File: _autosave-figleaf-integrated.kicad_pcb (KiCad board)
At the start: 2 copper layers, 145 x 105 mm, 62 parts, among them J2 HRO_TYPE-C-31-M-14, J3 Battery, J9 TC2030_SWD, Q2 2N7002, SW1 PWR, SW2 RST, U1 SRV05-4, U10 MAX17048, U3 BQ24075, U8 nRF52840_moko_mk08

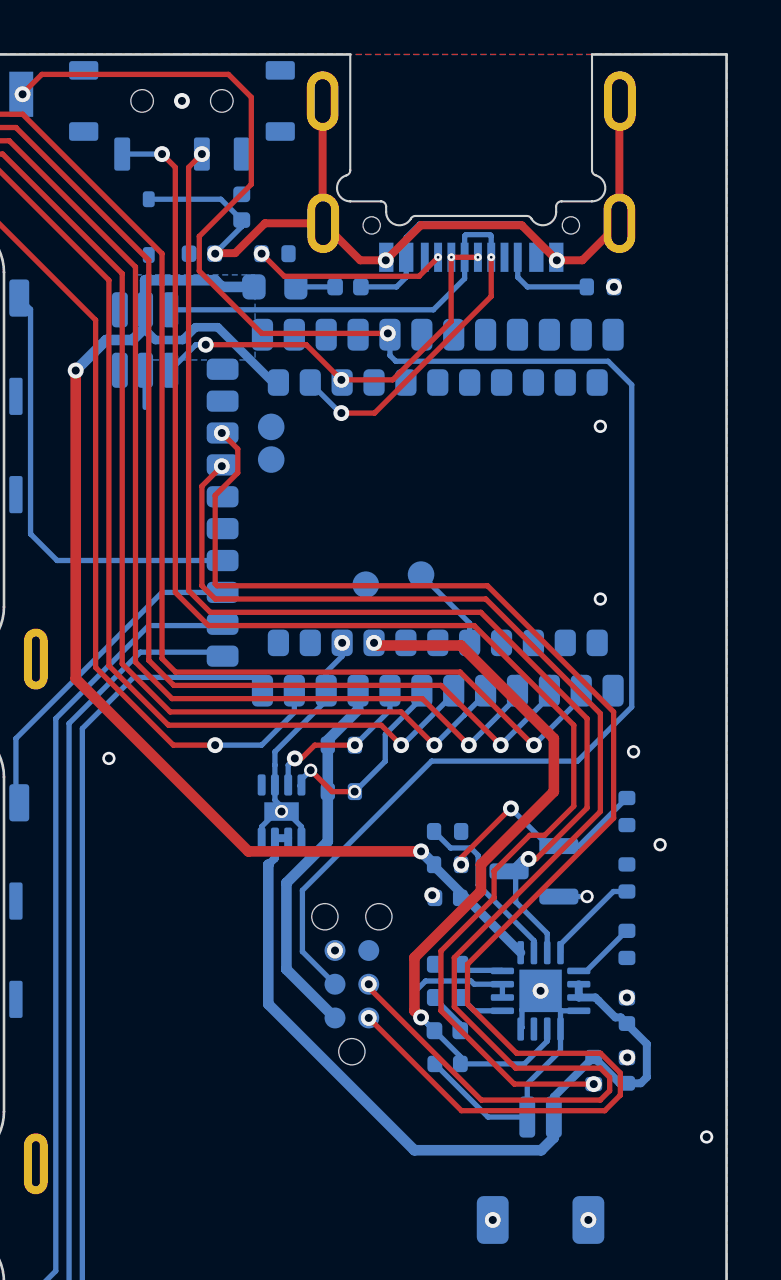
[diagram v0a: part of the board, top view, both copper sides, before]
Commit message: remove vias from smd pads
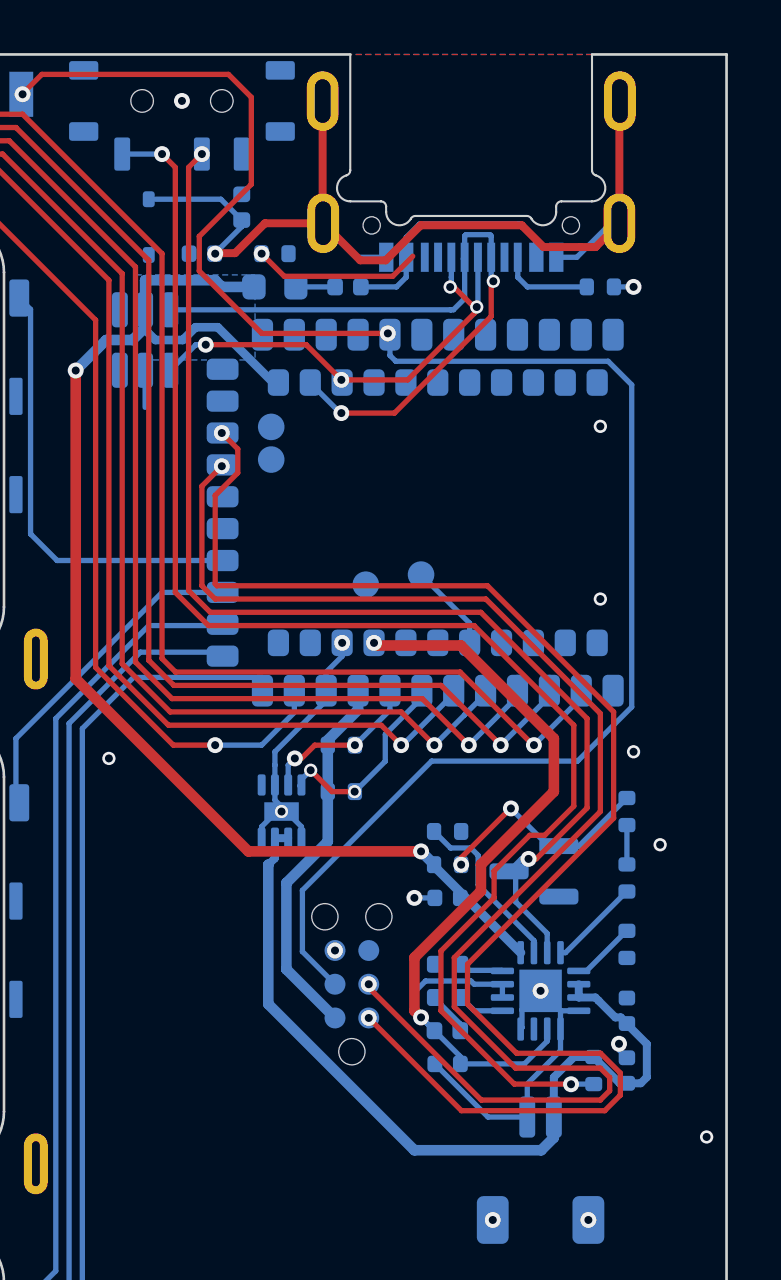
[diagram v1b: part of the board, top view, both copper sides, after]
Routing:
- net Earth: track 32.4 -> 37.8 mm, vias 3 -> 1
- net GND_L: track 28.4 -> 31.0 mm, vias 19 -> 17
- net USB-D-: track 15.8 -> 18.0 mm
- net USB-D+: track 25.7 -> 26.8 mm
- net Net-(J2-CC1): track 7.29 -> 6.35 mm, vias 2 -> 1
